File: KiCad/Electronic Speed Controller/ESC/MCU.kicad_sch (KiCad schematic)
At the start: 16 parts, among them SW1 SW_DIP_x01, U1 STM32F405RGTx

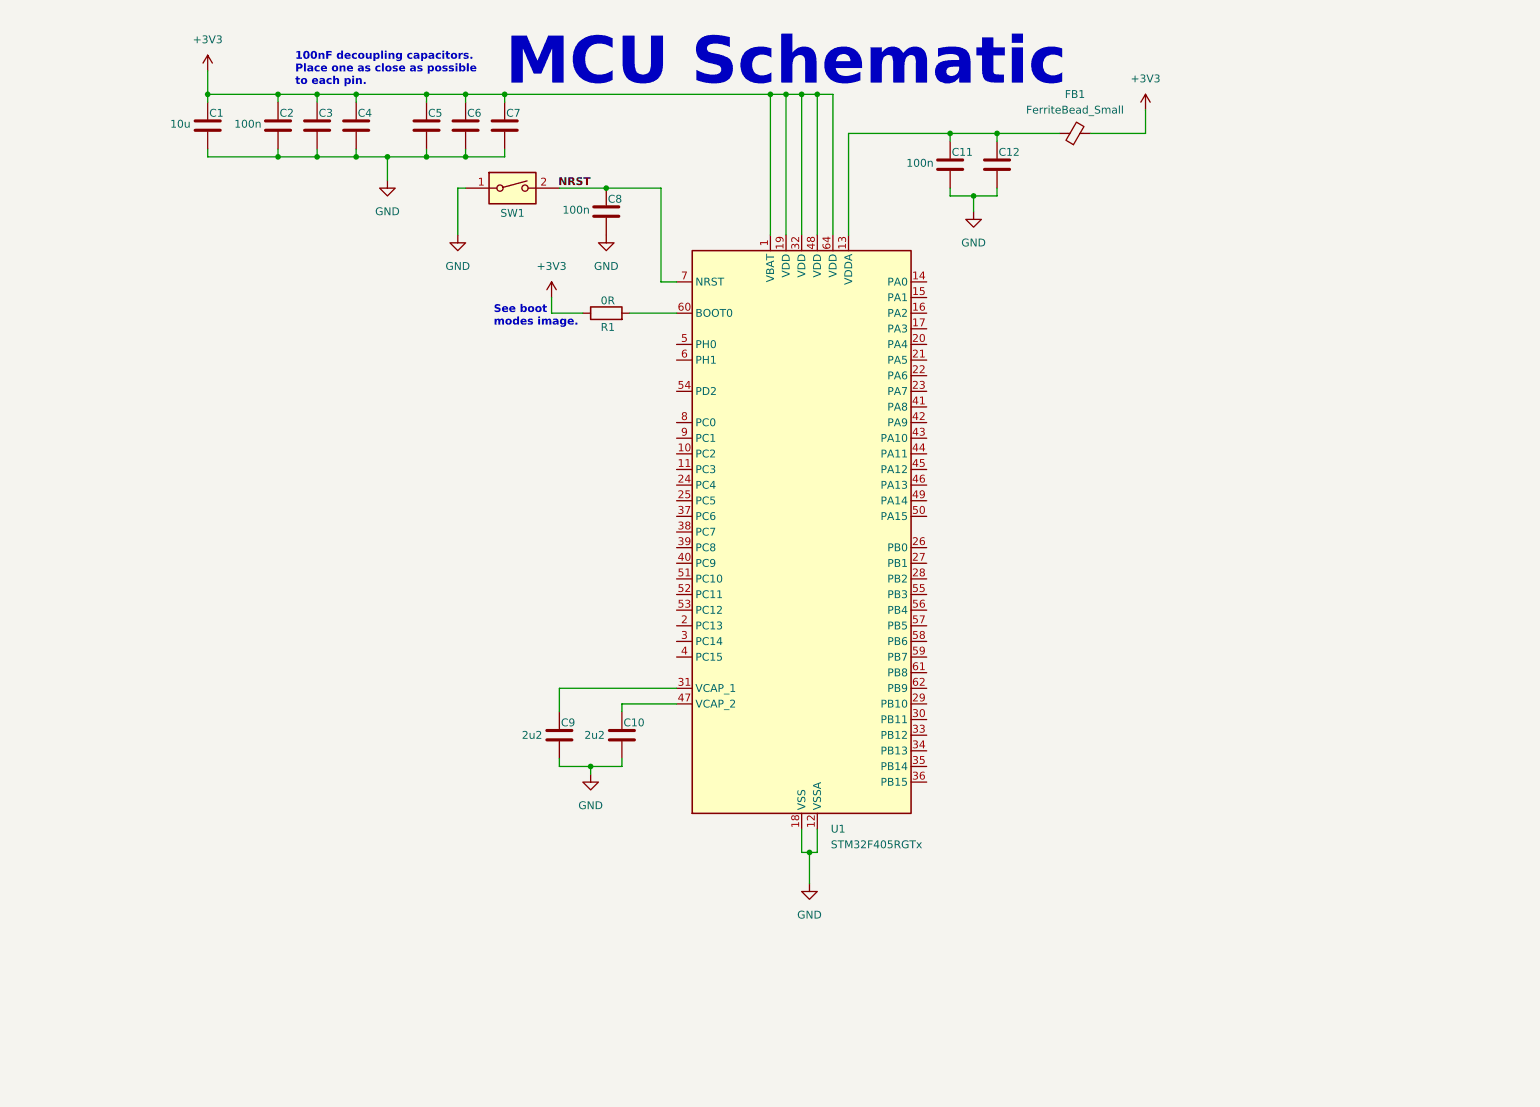
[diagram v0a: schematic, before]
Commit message: Update MCU schematic net labels
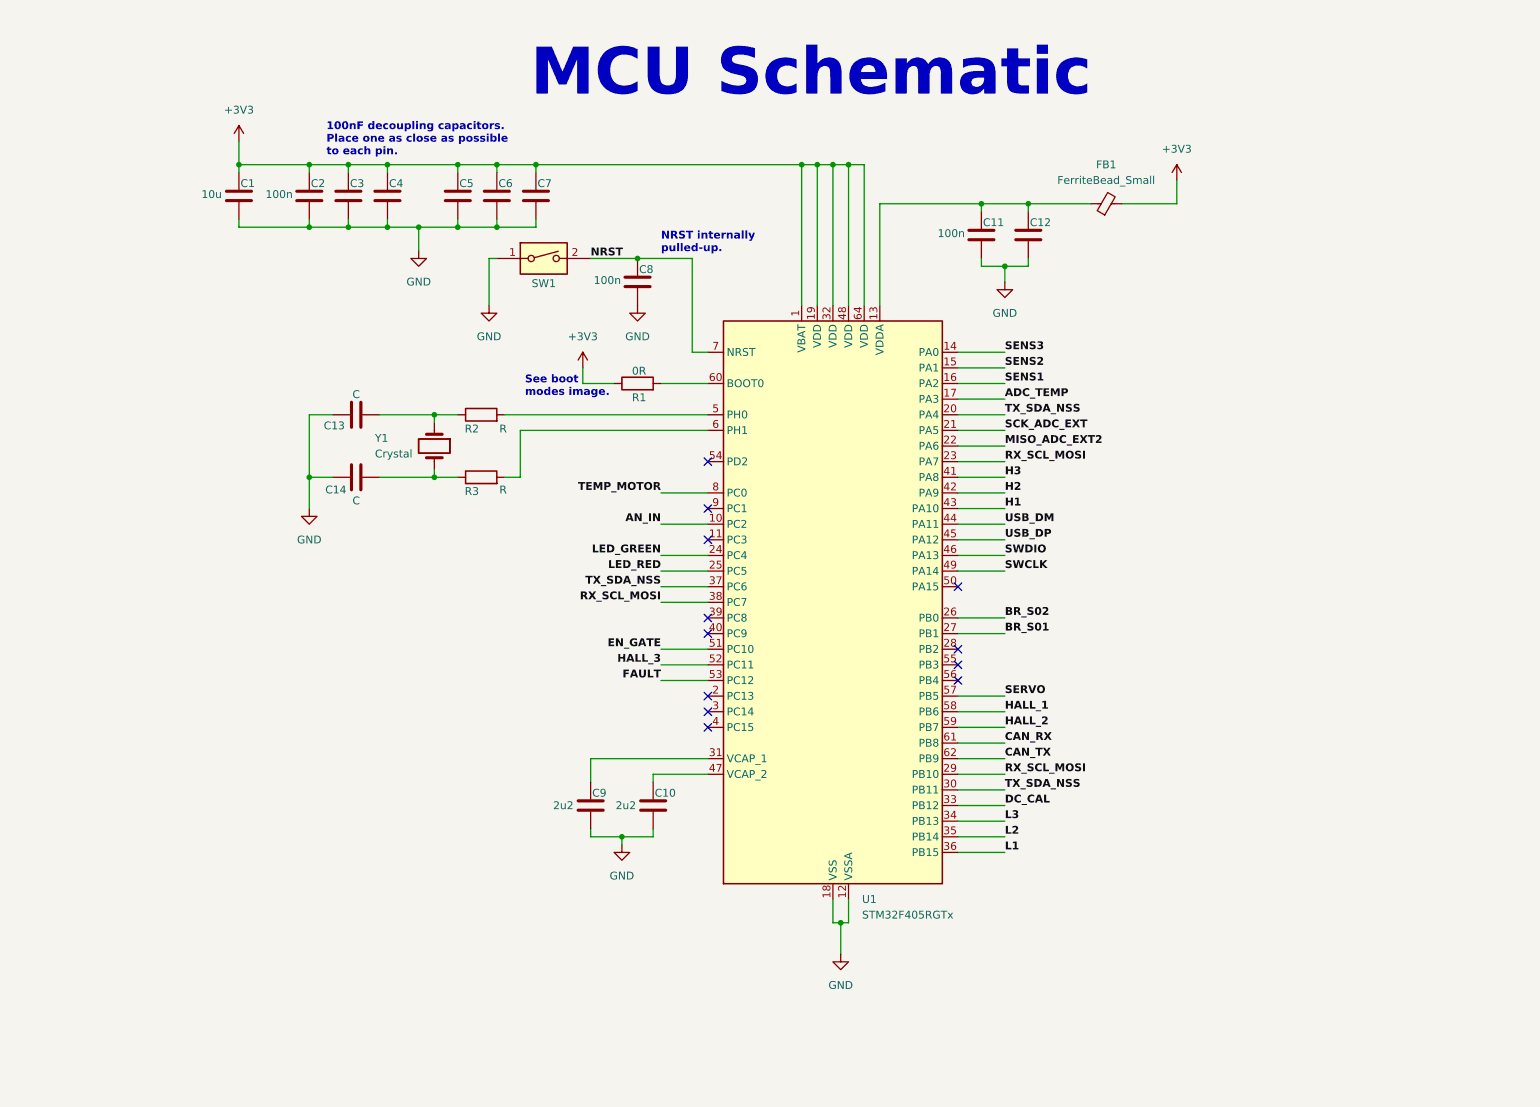
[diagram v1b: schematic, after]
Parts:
- added C13, C14: C, symbol Device:C
- added R2, R3: R, symbol Device:R
- added Y1: Crystal, symbol Device:Crystal
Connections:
- net GND: now also C13.1, C14.1
- net AN_IN: now reaches U1.10 (PC2)
- net SENS3: now reaches U1.14 (PA0)
- net SENS2: now reaches U1.15 (PA1)
- net SENS1: now reaches U1.16 (PA2)
- net ADC_TEMP: now reaches U1.17 (PA3)
- net TX_SDA_NSS: now reaches U1.20 (PA4)
- net TX_SDA_NSS: now also U1.30 (PB11), U1.37 (PC6)
- net SCK_ADC_EXT: now reaches U1.21 (PA5)
- net MISO_ADC_EXT2: now reaches U1.22 (PA6)
- net RX_SCL_MOSI: now reaches U1.23 (PA7)
- net RX_SCL_MOSI: now also U1.29 (PB10), U1.38 (PC7)
- net LED_GREEN: now reaches U1.24 (PC4)
- net LED_RED: now reaches U1.25 (PC5)
- net BR_S02: now reaches U1.26 (PB0)
- net BR_S01: now reaches U1.27 (PB1)
- net DC_CAL: now reaches U1.33 (PB12)
- net L3: now reaches U1.34 (PB13)
- net L2: now reaches U1.35 (PB14)
- net L1: now reaches U1.36 (PB15)
- net H3: now reaches U1.41 (PA8)
- net H2: now reaches U1.42 (PA9)
- net H1: now reaches U1.43 (PA10)
- net USB_DM: now reaches U1.44 (PA11)
- net USB_DP: now reaches U1.45 (PA12)
- net SWDIO: now reaches U1.46 (PA13)
- net SWCLK: now reaches U1.49 (PA14)
- net at U1.5 (PH0): now also R2.2
- net EN_GATE: now reaches U1.51 (PC10)
- net HALL_3: now reaches U1.52 (PC11)
- net FAULT: now reaches U1.53 (PC12)
- net SERVO: now reaches U1.57 (PB5)
- net HALL_1: now reaches U1.58 (PB6)
- net HALL_2: now reaches U1.59 (PB7)
- net at U1.6 (PH1): now also R3.2
- net CAN_RX: now reaches U1.61 (PB8)
- net CAN_TX: now reaches U1.62 (PB9)
- net TEMP_MOTOR: now reaches U1.8 (PC0)
- new net: C14.2, R3.1, Y1.2
- new net: C13.2, R2.1, Y1.1
- no-connect marks 0 -> 12
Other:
- note added: "NRST internally pulled-up."
- moved on the sheet: C1, C10, C11, C12, C2, C3, C4, C5, C6, C7, C8, C9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

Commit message: Update MCU schematic
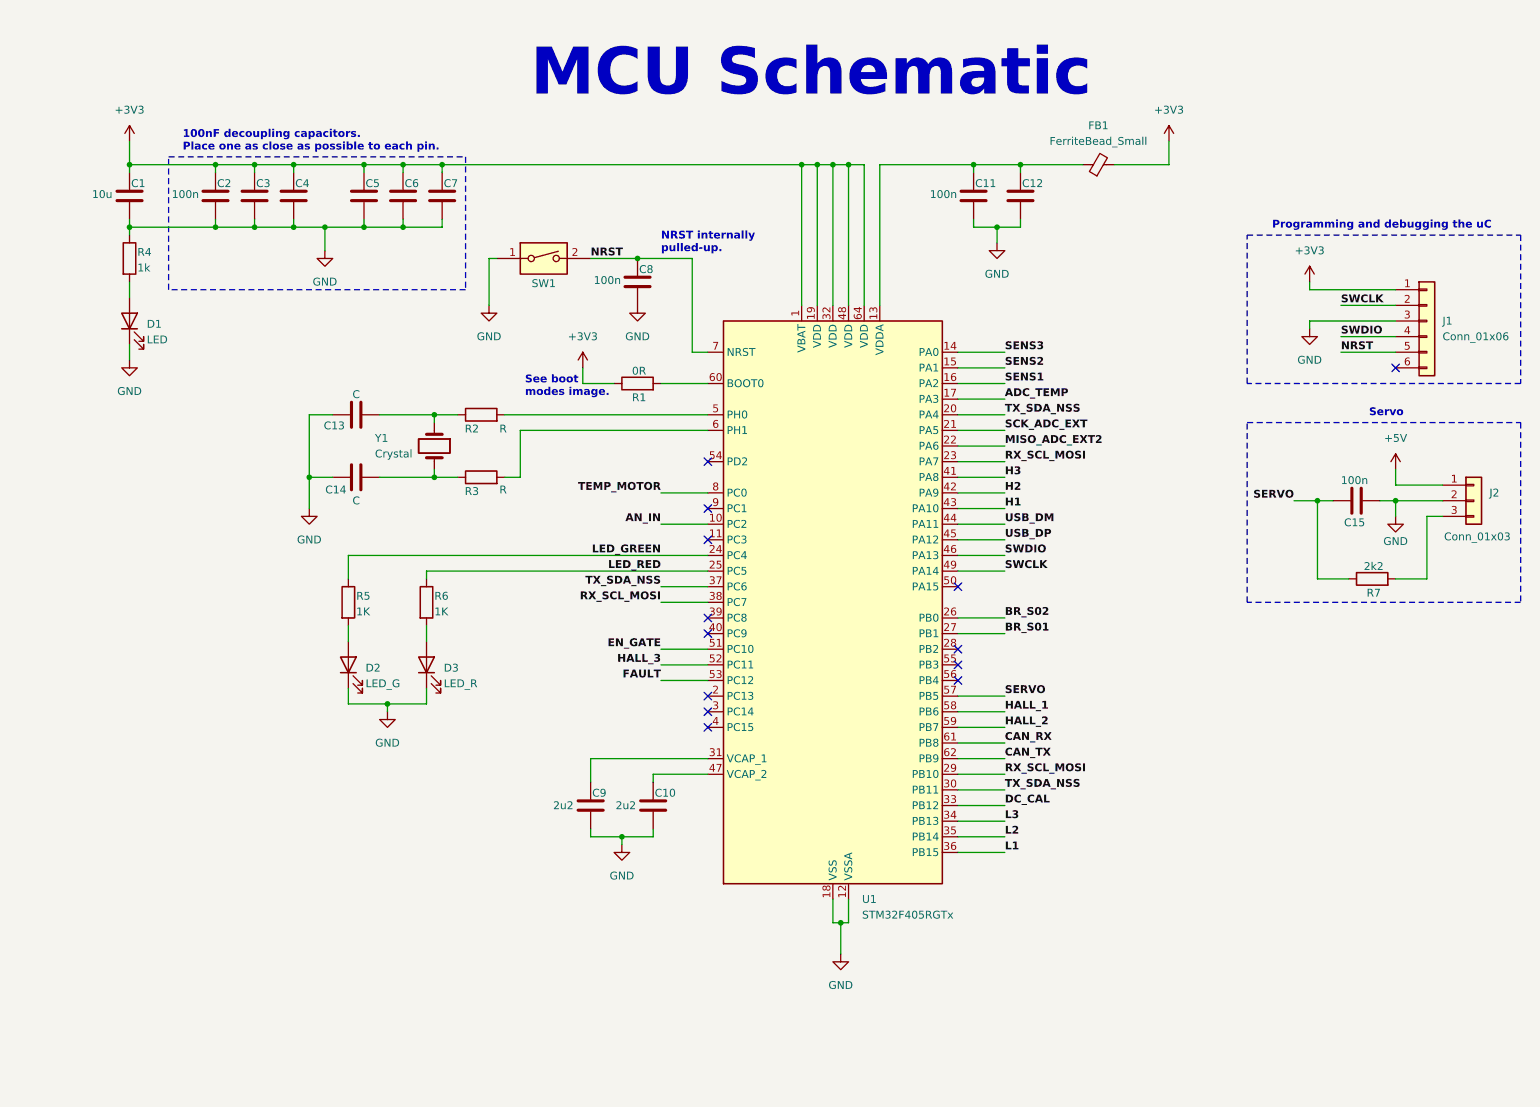
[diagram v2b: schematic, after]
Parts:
- added C15: 100n, symbol Device:C
- added D1: LED, symbol Device:LED
- added D2: LED_G, symbol Device:LED
- added D3: LED_R, symbol Device:LED
- added J1: Conn_01x06, symbol Connector_Generic:Conn_01x06
- added J2: Conn_01x03, symbol Connector_Generic:Conn_01x03
- added R4: 1k, symbol Device:R
- added R5, R6: 1K, symbol Device:R
- added R7: 2k2, symbol Device:R
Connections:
- net +3V3: now also J1.1 (Pin_1)
- net GND: now also C15.1, D1.1 (K), D2.1 (K), D3.1 (K), J1.3 (Pin_3), J2.2 (Pin_2), R4.1
- net LED_GREEN: now also R5.1
- net LED_RED: now also R6.1
- net NRST: now also J1.5 (Pin_5)
- net SERVO: now also C15.2, R7.1
- net SWCLK: now also J1.2 (Pin_2)
- net SWDIO: now also J1.4 (Pin_4)
- new net: D3.2 (A), R6.2
- new net: D2.2 (A), R5.2
- new net: J2.3 (Pin_3), R7.2
- new net: D1.2 (A), R4.2
- new net +5V: J2.1 (Pin_1)
- no-connect marks 12 -> 13
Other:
- note added: "Programming and debugging the uC"
- note added: "Servo"
- moved on the sheet: C1, C11, C12, C2, C3, C4, C5, C6, C7, FB1

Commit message: Update MCU schematic
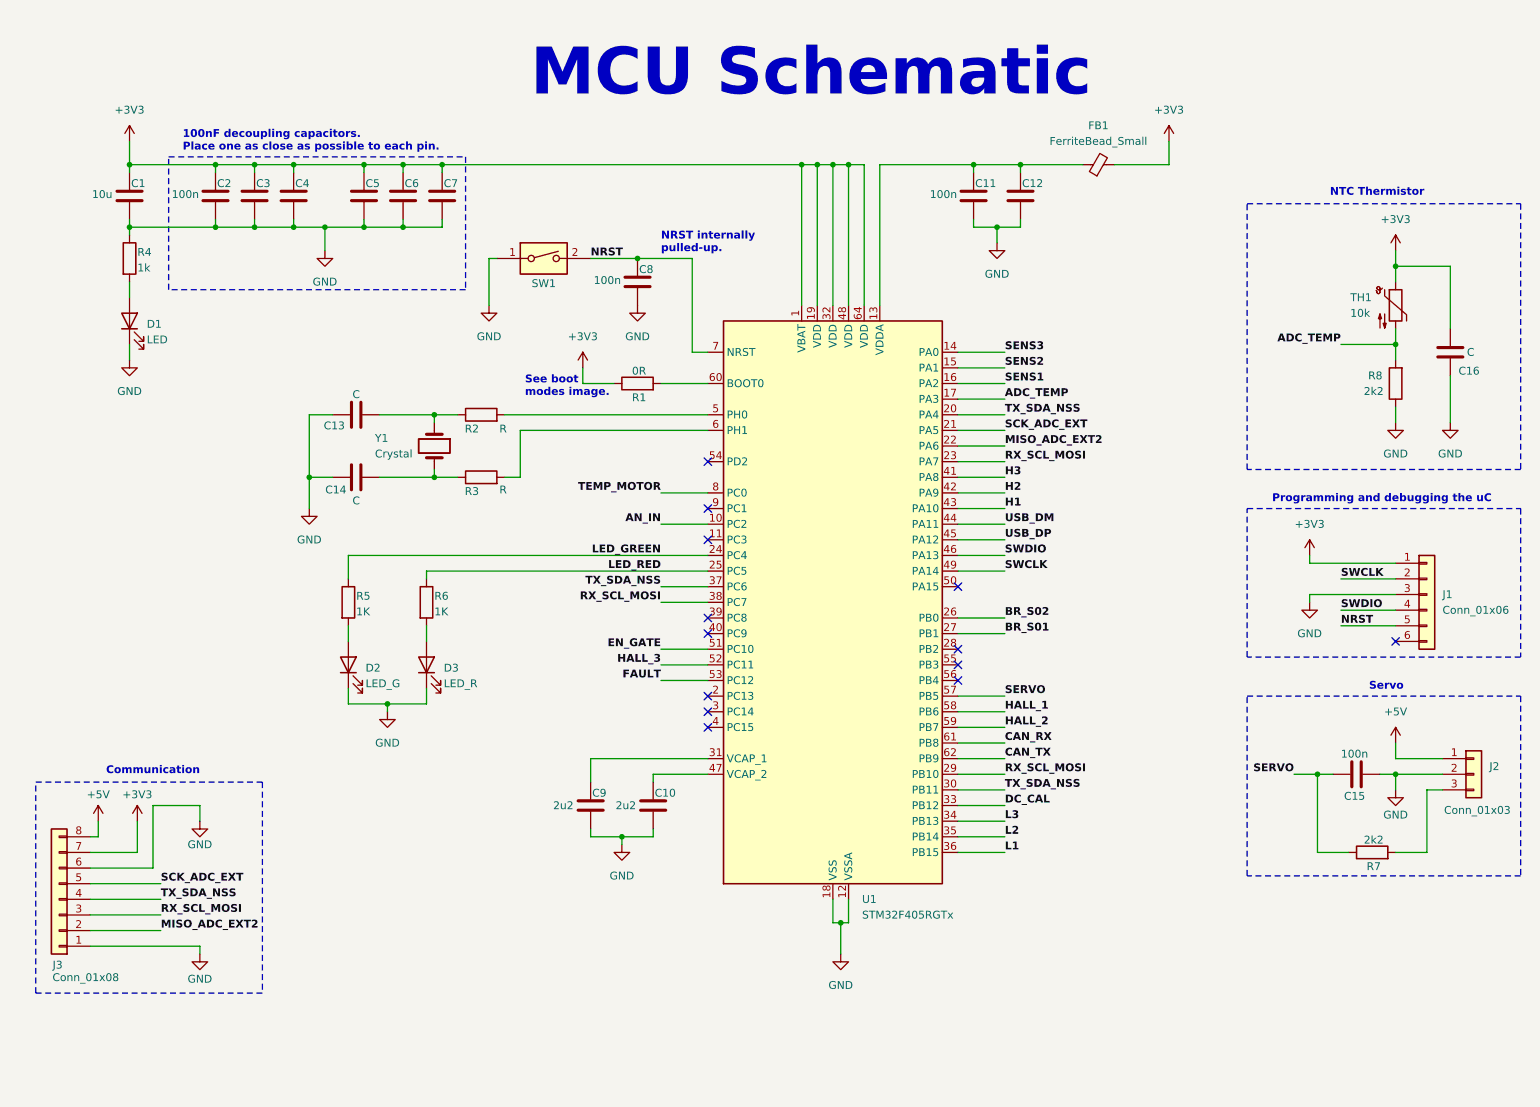
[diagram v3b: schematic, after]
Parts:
- added C16: C, symbol Device:C
- added J3: Conn_01x08, symbol Connector_Generic:Conn_01x08
- added R8: 2k2, symbol Device:R
- added TH1: 10k, symbol Device:Thermistor_NTC
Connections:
- net +3V3: now also C16.2, J3.7 (Pin_7), TH1.1
- net +5V: now also J3.8 (Pin_8)
- net ADC_TEMP: now also R8.2, TH1.2
- net GND: now also C16.1, J3.1 (Pin_1), J3.6 (Pin_6), R8.1
- net MISO_ADC_EXT2: now also J3.2 (Pin_2)
- net RX_SCL_MOSI: now also J3.3 (Pin_3)
- net SCK_ADC_EXT: now also J3.5 (Pin_5)
- net TX_SDA_NSS: now also J3.4 (Pin_4)
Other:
- note added: "Communication"
- note added: "NTC Thermistor"
- moved on the sheet: C15, J1, J2, R7

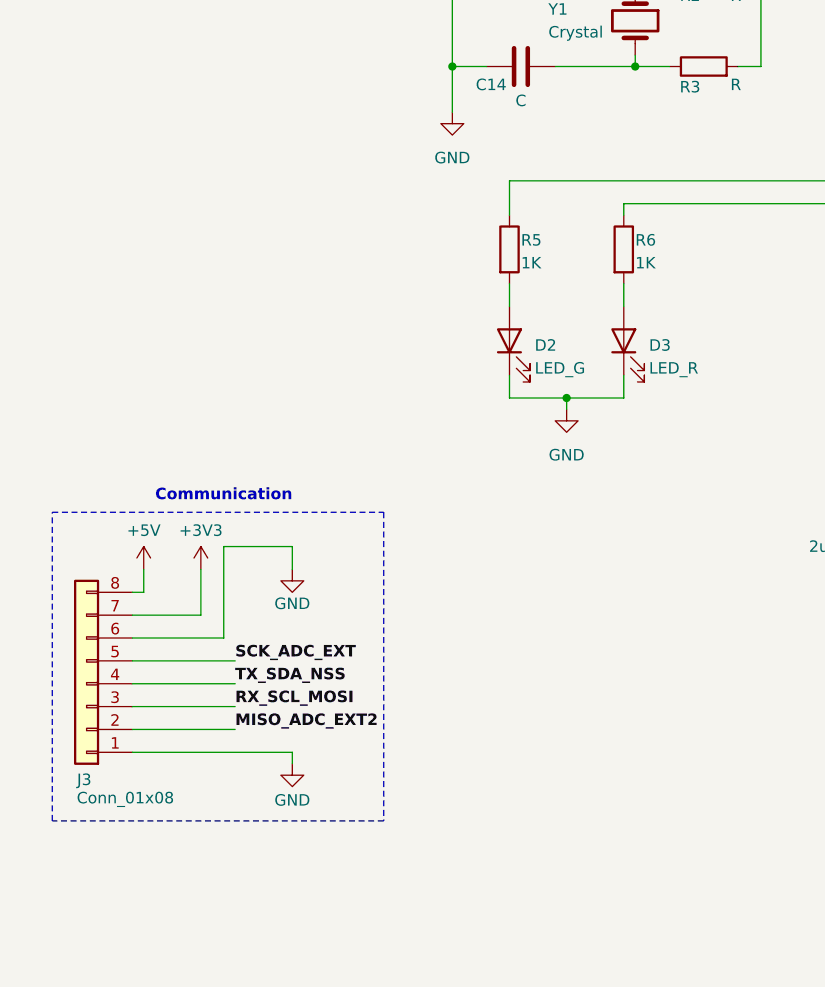
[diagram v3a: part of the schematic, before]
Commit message: Add voltage divider circuit to MCU schematic
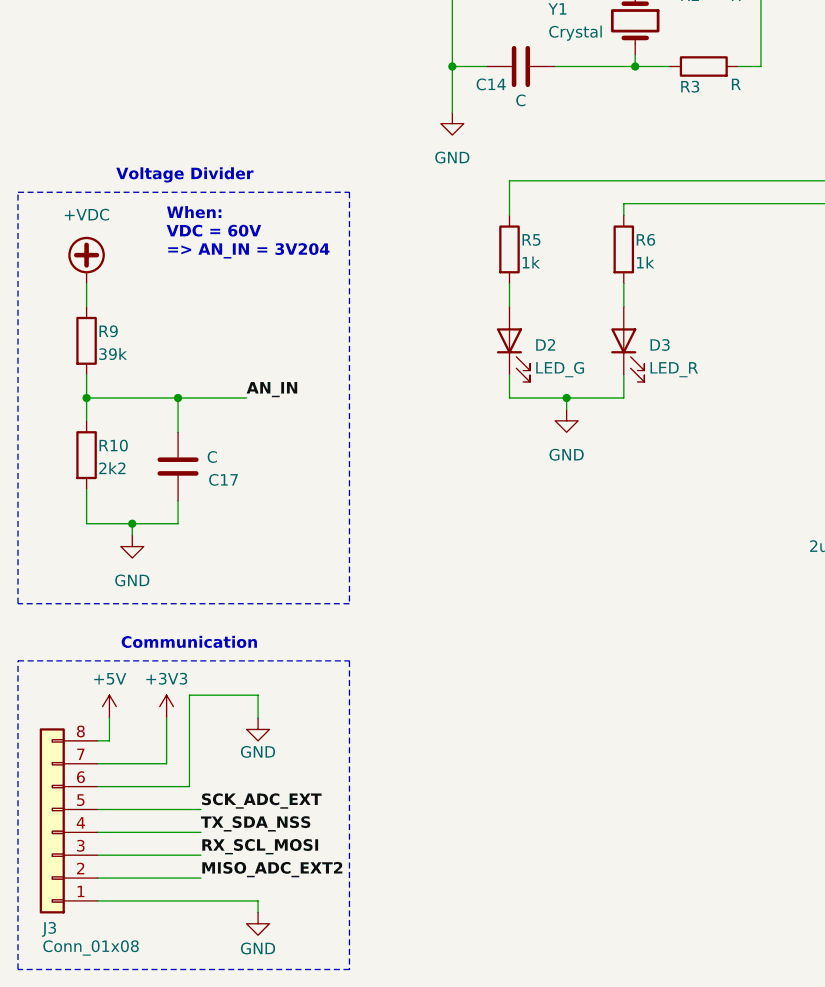
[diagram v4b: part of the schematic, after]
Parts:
- added C17: C, symbol Device:C
- added R10: 2k2, symbol Device:R
- added R9: 39k, symbol Device:R
- R5, R6: value 1K -> 1k
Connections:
- net AN_IN: now also C17.1, R10.1, R9.2
- net GND: now also C17.2, R10.2
- new net +VDC: R9.1
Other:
- note added: "Voltage Divider"
- note added: "When: VDC = 60V => AN_IN = 3V204"
- moved on the sheet: J3
